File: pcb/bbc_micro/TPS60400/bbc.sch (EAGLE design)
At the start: 24 parts, among them U2 LM2776

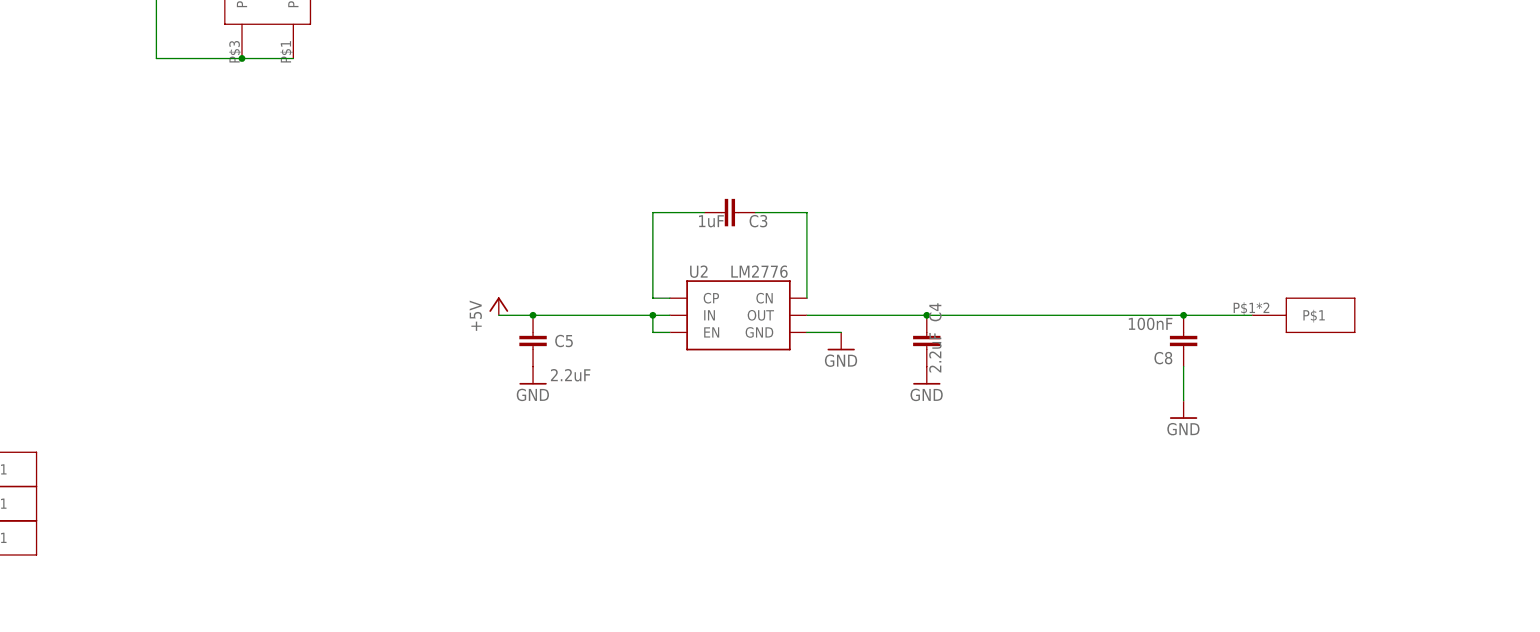
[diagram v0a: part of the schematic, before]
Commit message: changed bbc micro PCB with LM2776
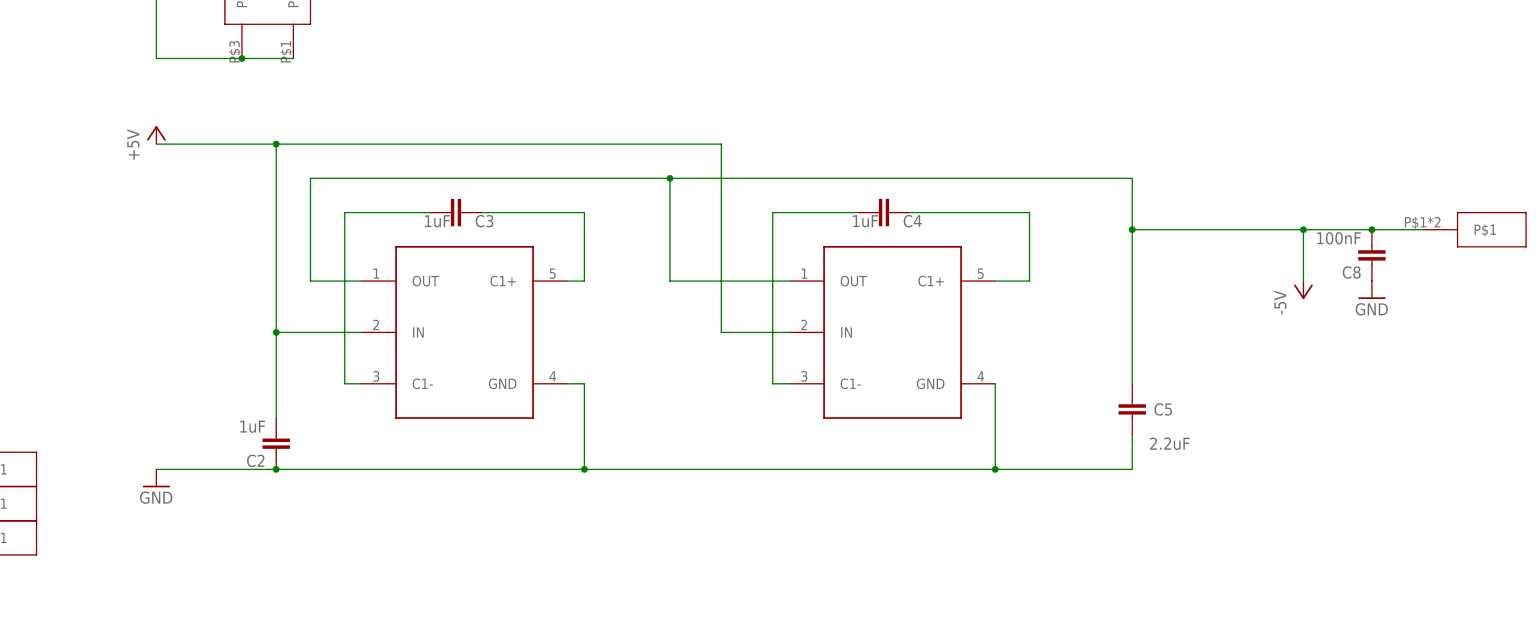
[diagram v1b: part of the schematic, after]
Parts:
- removed U2: LM2776, dword1511-pmic-dcdc:LM2776
- added C2: 1uF, clock:CAP0805
- added U1, U3: TPS60400DVBR, TPS6040x:TPS60400DVBR
- C4: value 2.2uF -> 1uF
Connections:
- new net -5V: C5.1, C8.2, U$5.P$1, U1.OUT, U3.OUT
- new net N$5: C4.1, U1.C1+
- net +5V: now also C2.2, U1.IN, U3.IN; no longer C5.1, U2.EN, U2.IN
- net GND: now also C2.1, U1.GND, U3.GND; no longer C4.2, U2.GND
- net N$2: now also U3.C1-; no longer U2.CP
- net N$3: now also U3.C1+; no longer U2.CN
- net N$4: now also C4.2, U1.C1-; no longer C4.1, C8.2, U$5.P$1, U2.OUT
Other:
- moved on the sheet: C3, C4, C5, C8
